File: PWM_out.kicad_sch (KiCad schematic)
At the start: 32 parts, among them J11 Conn_01x03_Pin, J12 Conn_01x03_Pin, J13 Conn_01x03_Pin, J14 Conn_01x03_Pin, J2 Conn_01x03_Pin, J3 Conn_01x03_Pin, J4 Conn_01x03_Pin, J5 Conn_01x03_Pin

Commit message: feat:убрал часть с батарейным питанием, убрал лишние элементы со старого проекта
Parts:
- removed C35, C36, C37, C38, C39, C40, C41, C42: 0.1u, Capacitor_SMD:C_0805_2012Metric_Pad1.18x1.45mm_HandSolder, symbol Device:C_Small
- removed J11, J12, J13, J14, J2, J3, J4, J5: Conn_01x03_Pin, Connector_PinHeader_2.54mm:PinHeader_1x03_P2.54mm_Vertical, symbol Connector:Conn_01x03_Pin
- removed R12, R13, R14, R15, R16, R17, R18, R19: 0, Resistor_SMD:R_0805_2012Metric_Pad1.20x1.40mm_HandSolder, symbol Device:R
- removed VD11, VD12, VD13, VD5, VD6, VD7, VD8, VD9: GSOT03C-E3-08, Package_TO_SOT_SMD:SOT-23, symbol TWS:GSOT03C-E3-08

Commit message: feaat: добавлены светодиоды, кнопки и недостающие элементы защиты питания
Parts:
- added D10, D11, D12, D13, D14, D8: LED, LED_THT:LED_D3.0mm, symbol Device:LED
- added Q3, Q4, Q5, Q6, Q7, Q8: PDTC143ET, Package_TO_SOT_SMD:SOT-23-3, symbol Transistors:PDTC143ET
- added R11, R12, R14, R16, R6, R9: 220, Resistor_SMD:R_0805_2012Metric_Pad1.20x1.40mm_HandSolder, symbol Device:R
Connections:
- new net: D8.1 (K), Q3.3 (C)
- new net: D11.1 (K), Q5.3 (C)
- new net: D13.1 (K), Q6.3 (C)
- new net: D13.2 (A), R12.2
- new net: D12.1 (K), Q7.3 (C)
- new net: D12.2 (A), R14.2
- new net: D14.2 (A), R16.2
- new net: D8.2 (A), R9.2
- new net: D10.1 (K), Q4.3 (C)
- new net: D11.2 (A), R11.2
- new net: D14.1 (K), Q8.3 (C)
- new net: D10.2 (A), R6.2
- new net +5V: R11.1, R12.1, R14.1, R16.1, R6.1, R9.1
- new net DO1: Q3.1 (B)
- new net DO2: Q4.1 (B)
- new net DO3: Q5.1 (B)
- new net DO4: Q6.1 (B)
- new net DO5: Q7.1 (B)
- new net DO6: Q8.1 (B)
- new net GND: Q3.2 (E), Q4.2 (E), Q5.2 (E), Q6.2 (E), Q7.2 (E), Q8.2 (E)

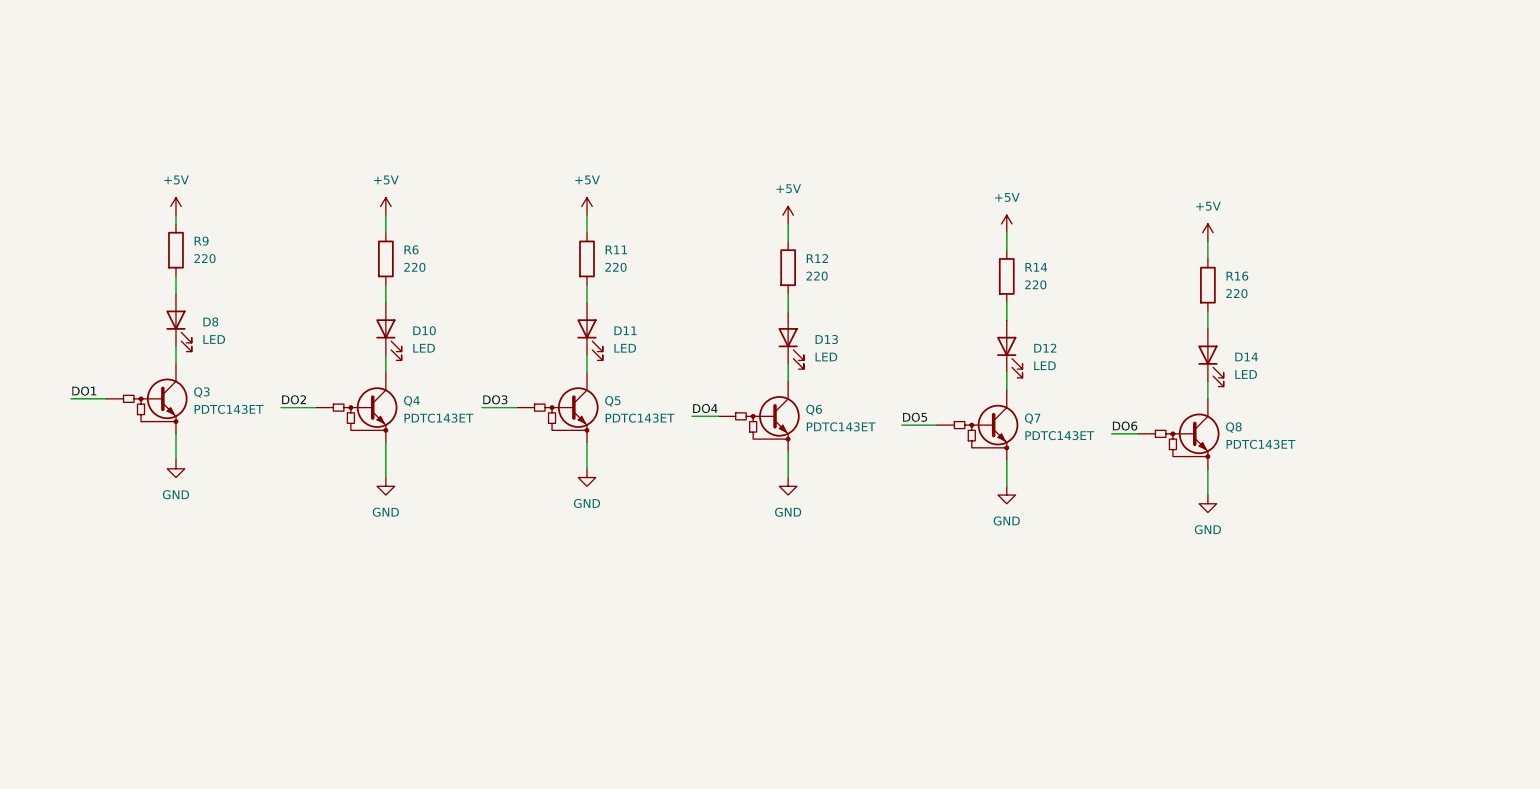
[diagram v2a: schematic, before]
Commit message: feat: добавлены глобальные линии связи, удалены линии связи со старого проекта
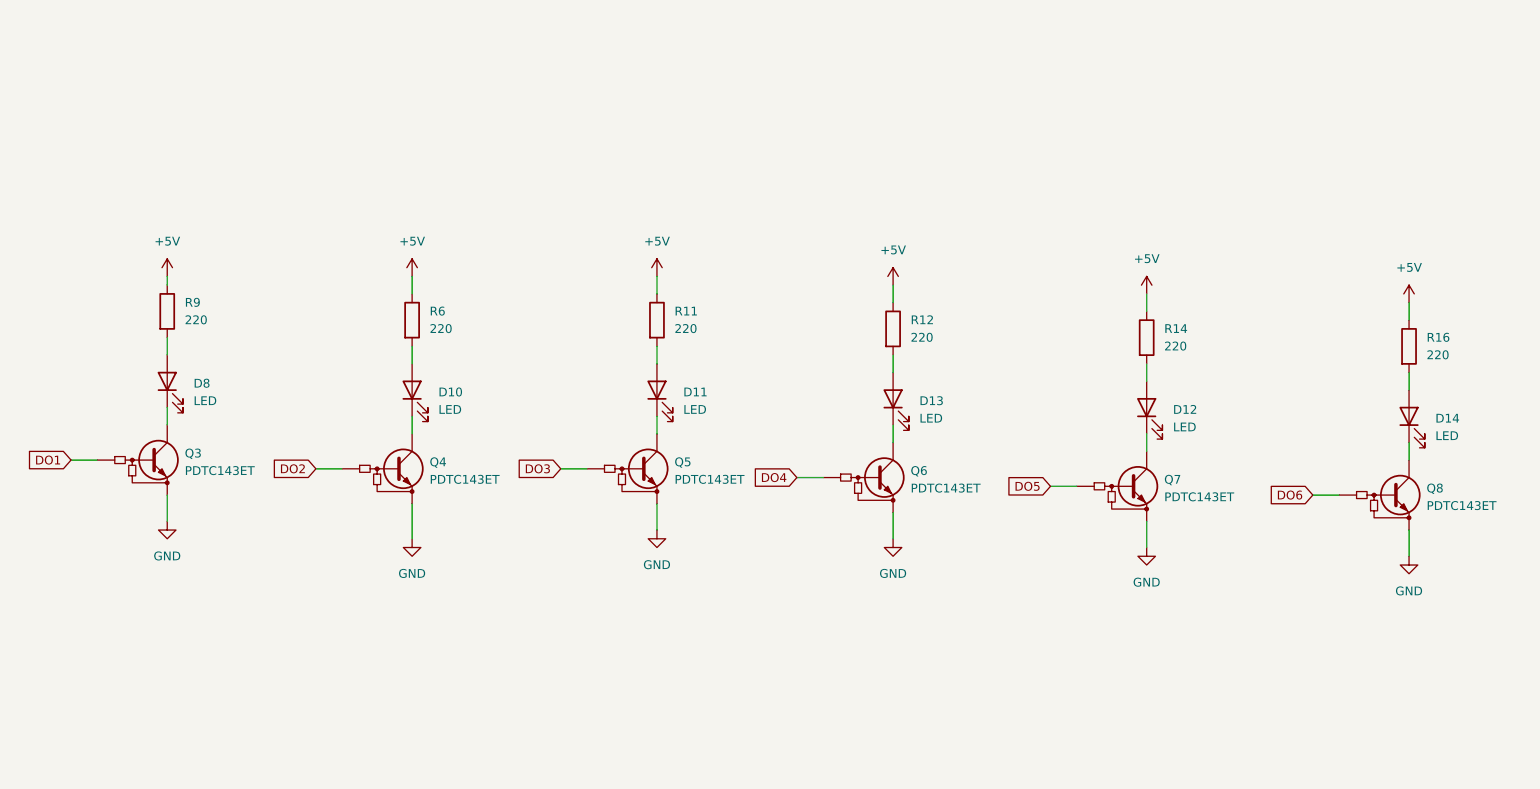
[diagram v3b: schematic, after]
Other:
- moved on the sheet: D10, D11, D12, D13, D14, D8, Q3, Q4, Q5, Q6, Q7, Q8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

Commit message: feat: добавлены светодиоды
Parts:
- added D16, D17, D18, D19: LED, LED_THT:LED_D3.0mm, symbol Device:LED
- added Q10, Q11, Q12, Q9: PDTC143ET, Package_TO_SOT_SMD:SOT-23-3, symbol Transistors:PDTC143ET
- added R10, R17, R18, R19: 220, Resistor_SMD:R_0805_2012Metric_Pad1.20x1.40mm_HandSolder, symbol Device:R
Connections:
- net +5V: now also R10.1, R17.1, R18.1, R19.1
- net GND: now also Q10.2 (E), Q11.2 (E), Q12.2 (E), Q9.2 (E)
- new net: D16.1 (K), Q9.3 (C)
- new net: D16.2 (A), R10.2
- new net: D18.2 (A), R18.2
- new net: D19.2 (A), R19.2
- new net: D19.1 (K), Q12.3 (C)
- new net: D17.1 (K), Q10.3 (C)
- new net: D17.2 (A), R17.2
- new net: D18.1 (K), Q11.3 (C)
- new net DO10: Q12.1 (B)
- new net DO7: Q9.1 (B)
- new net DO8: Q10.1 (B)
- new net DO9: Q11.1 (B)
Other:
- moved on the sheet: D10, D11, D12, D13, D14, D8, Q3, Q4, Q5, Q6, Q7, Q8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

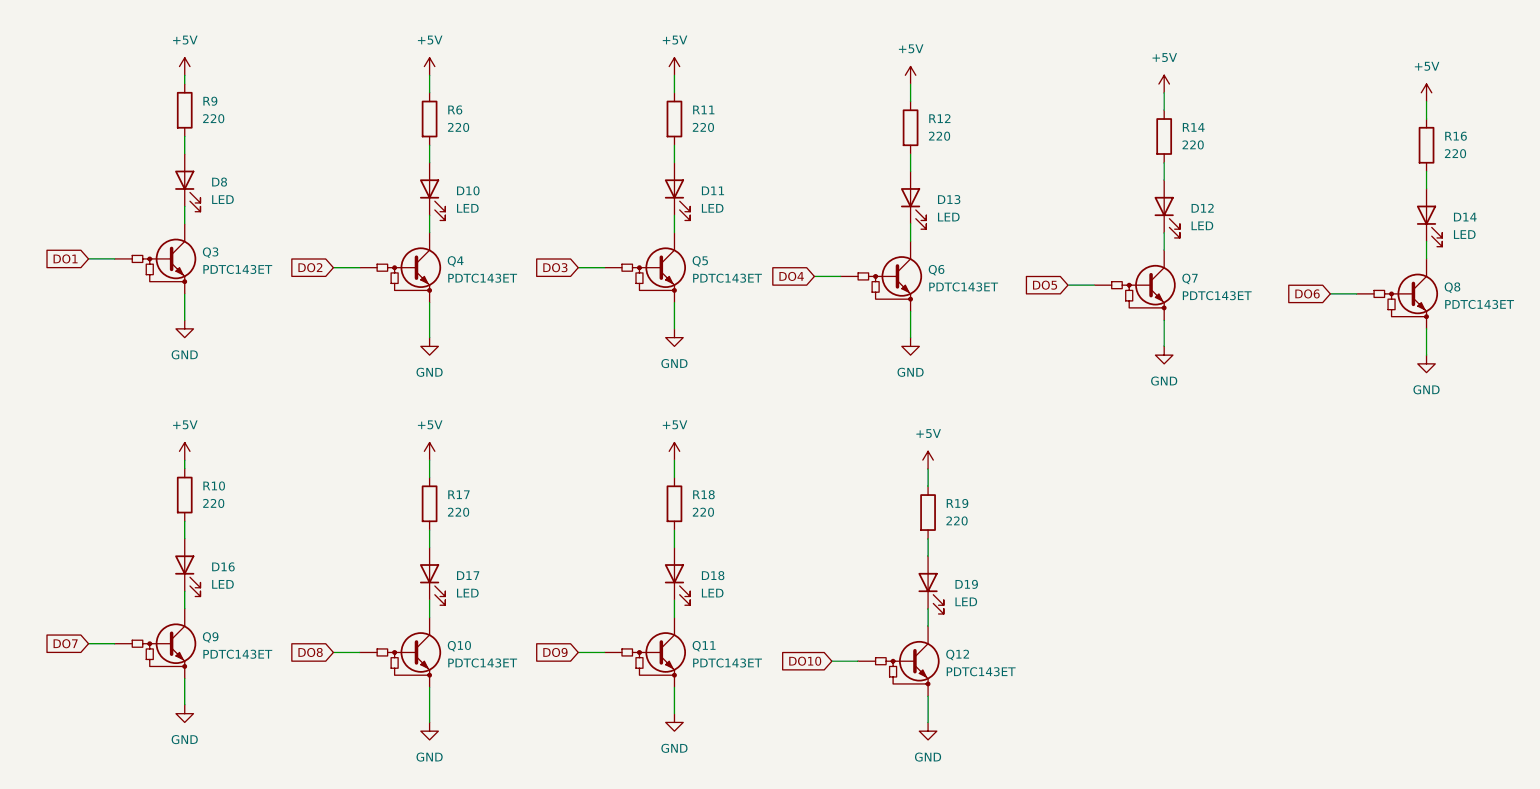
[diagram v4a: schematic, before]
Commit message: feat: расположены основные узлы модуля на печатной плате
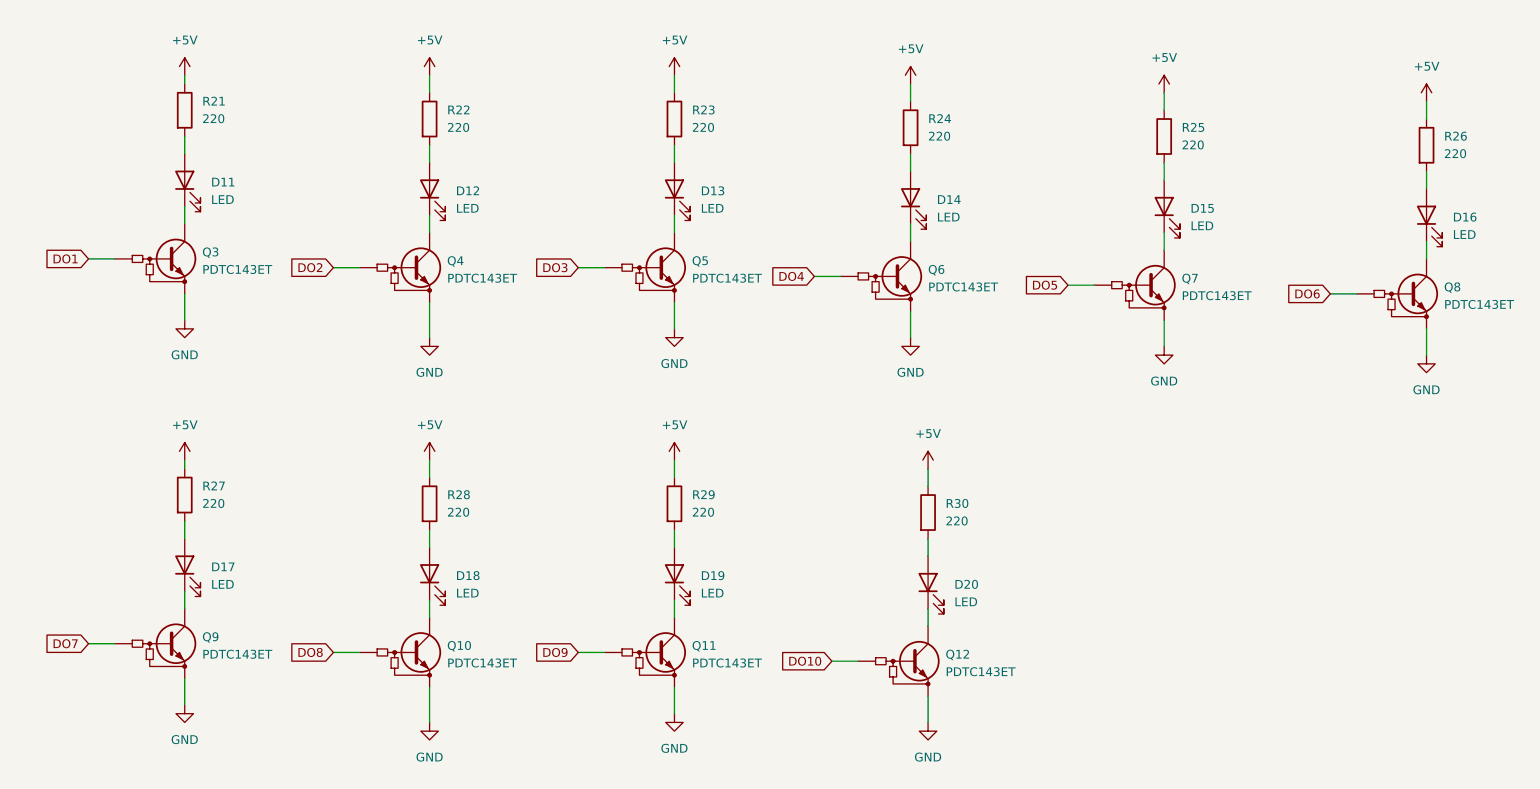
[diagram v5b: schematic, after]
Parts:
- renumbered D8 to D11, D10 to D12, D11 to D13, D13 to D14, D12 to D15, D14 to D16, D16 to D17, D17 to D18, D18 to D19, D19 to D20, R9 to R21, R6 to R22, R11 to R23, R12 to R24, R14 to R25, R16 to R26, R10 to R27, R17 to R28, R18 to R29, R19 to R30

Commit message: feat: добавлена микросхема для коммутации светодиодов
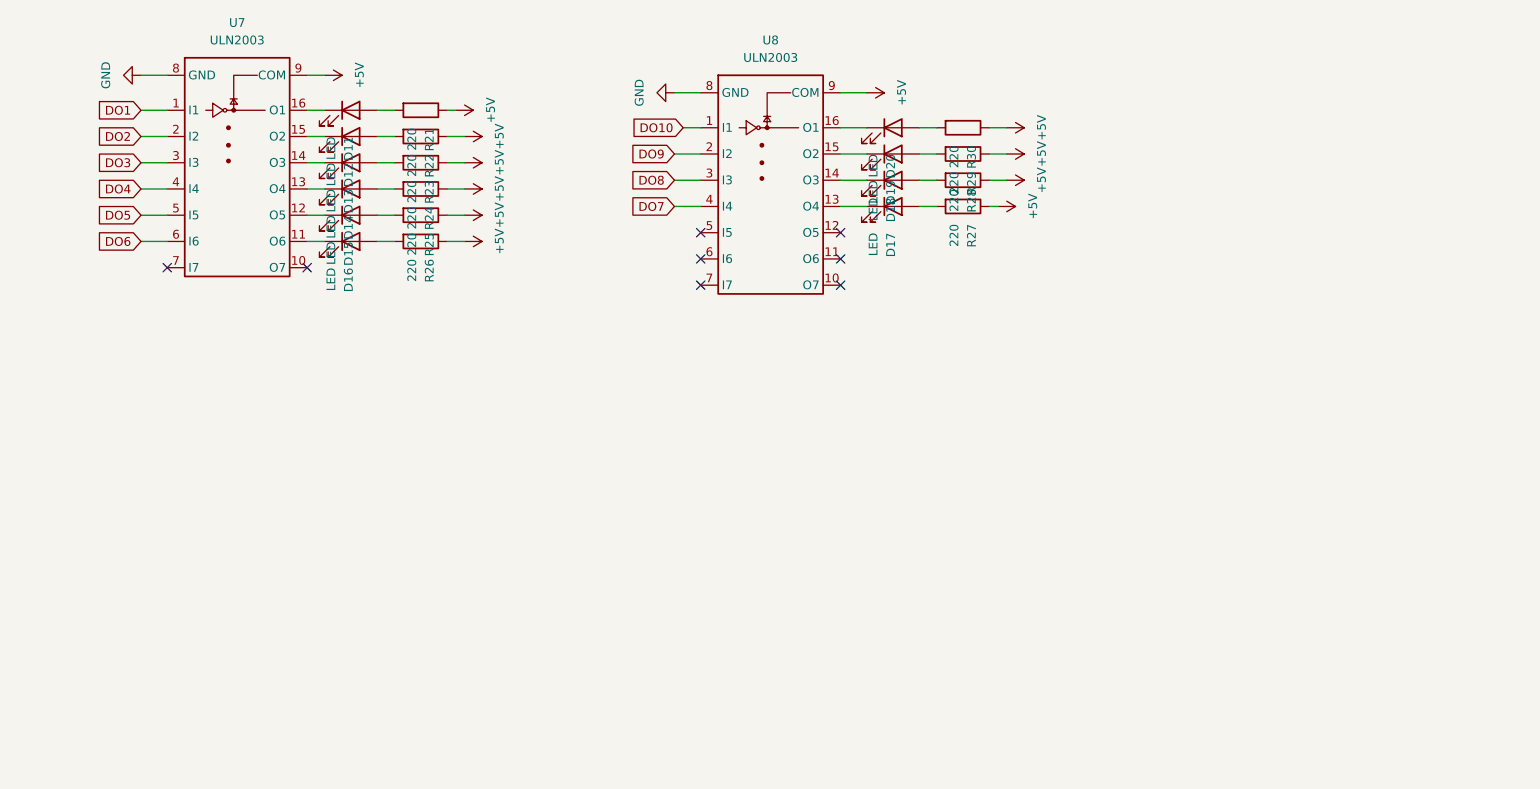
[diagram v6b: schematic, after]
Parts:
- removed Q10, Q11, Q12, Q3, Q4, Q5, Q6, Q7, Q8, Q9: PDTC143ET, Package_TO_SOT_SMD:SOT-23-3, symbol Transistors:PDTC143ET
- added U7, U8: ULN2003, Package_SO:SO-16_3.9x9.9mm_P1.27mm, symbol Transistor_Array:ULN2003
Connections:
- net +5V: now also U7.9 (COM), U8.9 (COM)
- net DO1: now also U7.1 (I1)
- net DO10: now also U8.1 (I1)
- net DO2: now also U7.2 (I2)
- net DO3: now also U7.3 (I3)
- net DO4: now also U7.4 (I4)
- net DO5: now also U7.5 (I5)
- net DO6: now also U7.6 (I6)
- net DO7: now also U8.4 (I4)
- net DO8: now also U8.3 (I3)
- net DO9: now also U8.2 (I2)
- net GND: now also U7.8 (GND), U8.8 (GND)
- net at D11.1 (K): now also U7.16 (O1)
- net at D13.1 (K): now also U7.14 (O3)
- net at D14.1 (K): now also U7.13 (O4)
- net at D15.1 (K): now also U7.12 (O5)
- net at D17.1 (K): now also U8.13 (O4)
- net at D12.1 (K): now also U7.15 (O2)
- net at D20.1 (K): now also U8.16 (O1)
- net at D18.1 (K): now also U8.14 (O3)
- net at D16.1 (K): now also U7.11 (O6)
- net at D19.1 (K): now also U8.15 (O2)
- no-connect marks 0 -> 8
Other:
- moved on the sheet: D11, D12, D13, D14, D15, D16, D17, D18, D19, D20, R21, R22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
